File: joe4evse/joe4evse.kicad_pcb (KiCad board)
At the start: 2 copper layers, 100 x 100 mm, 74 parts, among them J1 USB_B_Micro, J10 Conn_01x02, J11 Conn_01x02, J2 Conn_01x03, J3 Conn_01x03, J4 Conn_01x02, J5 Conn_01x02, J6 CONNFLY_Elec_DS1129-04-S8B0P-X, J7 8P8C_LED_Shielded, J8 Conn_01x02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

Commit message: joe/pcb: Routing done
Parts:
- added REF**: Symbol_Highvoltage_Type1_CopperTop_Small, Symbol:Symbol_Highvoltage_Type1_CopperTop_Small, F.Cu at (182.4, 54.0)
- J5: value Conn_01x02 -> Conn_01x03; footprint Connector_JST:JST_NV_B02P-NV_1x02_P5.00mm_Vertical -> Connector_JST:JST_NV_B03P-NV_1x03_P5.00mm_Vertical
- moved J8 53.5 mm to (147.5, 77.9)
- moved D7 14.0 mm to (192.0, 114.0)
- moved D8 14.0 mm to (192.0, 106.0)
- moved D9 14.0 mm to (192.0, 98.0)
- moved J10 14.0 mm to (197.0, 106.0)
- moved J11 14.0 mm to (197.0, 98.0)
- moved J9 14.0 mm to (197.0, 114.0)
- moved Q1 14.0 mm to (189.0, 116.0)
- moved Q2 14.0 mm to (189.0, 108.0)
- moved Q3 14.0 mm to (189.0, 100.0)
- moved R7 14.0 mm to (189.0, 97.0)
- moved R8 14.0 mm to (189.0, 113.0)
- moved R9 14.0 mm to (189.0, 105.0)
- moved D11 10.0 mm to (176.0, 77.0)
- moved J5 10.0 mm to (194.0, 77.0)
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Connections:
- J5 pad 2: /evse/AC_TEST_IN1 -> /evse/AC_TEST_N
- U7 pad 2: GND -> /evse/AC_TEST_N
- U7 pad 3: GND -> /evse/AC_TEST_N
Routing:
- net +3V3: track 0.00 -> 292.6 mm, vias 0 -> 12
- net +12V: track 0.00 -> 179.3 mm, vias 0 -> 3
- net +5V: track 0.00 -> 167.6 mm, vias 0 -> 3
- net /RELAY_RCMB: track 0.00 -> 80.9 mm, vias 0 -> 2
- net /MOD_EN: track 0.00 -> 80.6 mm
- net /RELAY_JACK: track 0.00 -> 75.0 mm, vias 0 -> 4
- net /RELAY_AC: track 0.00 -> 74.1 mm, vias 0 -> 2
- net /evse/AC_TEST1: track 0.00 -> 73.9 mm
- net /NFC_~RST: track 0.00 -> 72.2 mm, vias 0 -> 2
- net /evse/AC_TEST0: track 0.00 -> 69.9 mm
- net /LED_~CS: track 0.00 -> 68.2 mm, vias 0 -> 2
- net /SCLK: track 0.00 -> 67.4 mm
- net /fipy/RCMB_AC_30mA: track 0.00 -> 66.6 mm
- net /NFC_IRQ: track 0.00 -> 66.2 mm, vias 0 -> 1
- net /NFC_~CS: track 0.00 -> 65.8 mm, vias 0 -> 2
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- added copper zone on B.Cu, net GND
- added copper zone on F.Cu, net GND
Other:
- outline, holes or cut-outs redrawn
- board text added: "A <-> B"
- board text added: "Dalton EVSE "Joe" Board rev. 1.0 (c) Tuetuopay 2019"
- board text added: "High voltage"
- board text added: "PP | Pilot"
- board text added: "RCMB relay AC cutoff relay EV Jack relay"
- board text added: "To Averell"
- board text added: "To William"

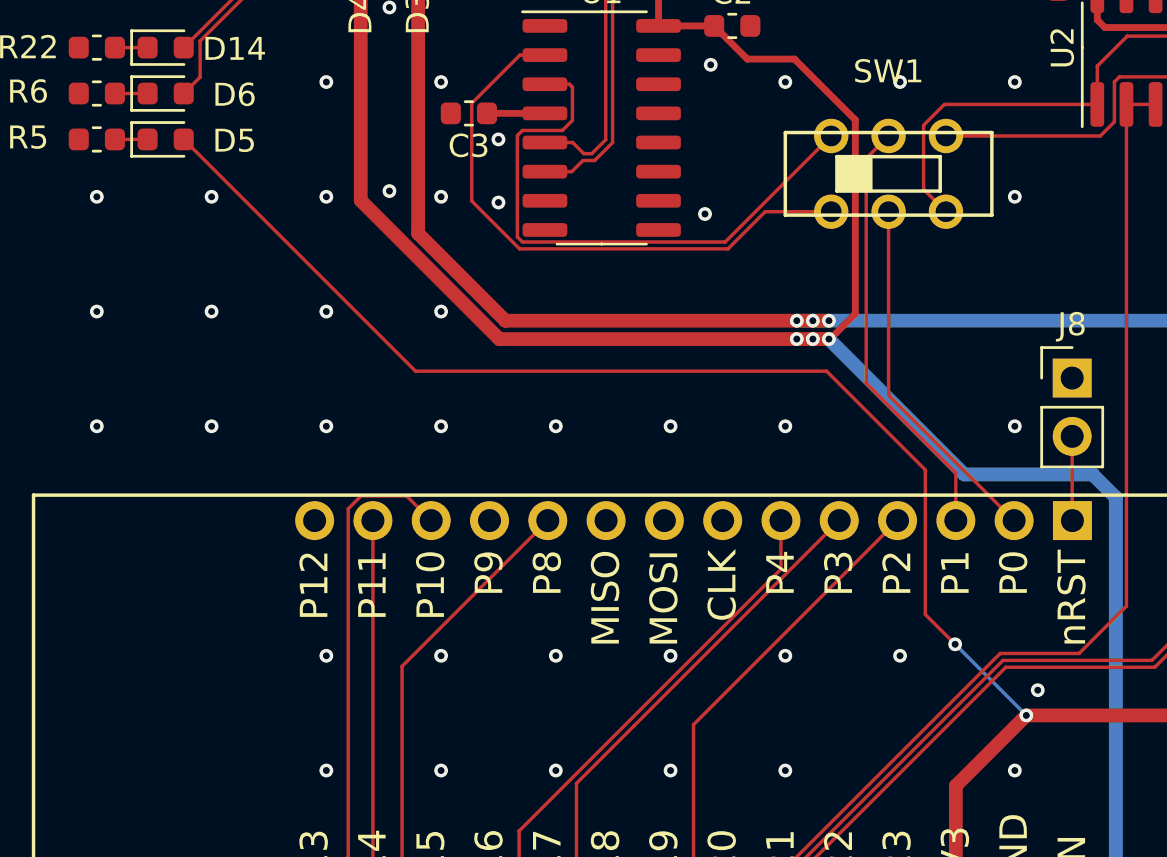
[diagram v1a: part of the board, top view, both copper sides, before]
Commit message: joe/{sch, pcb}: Add missing temp sensor
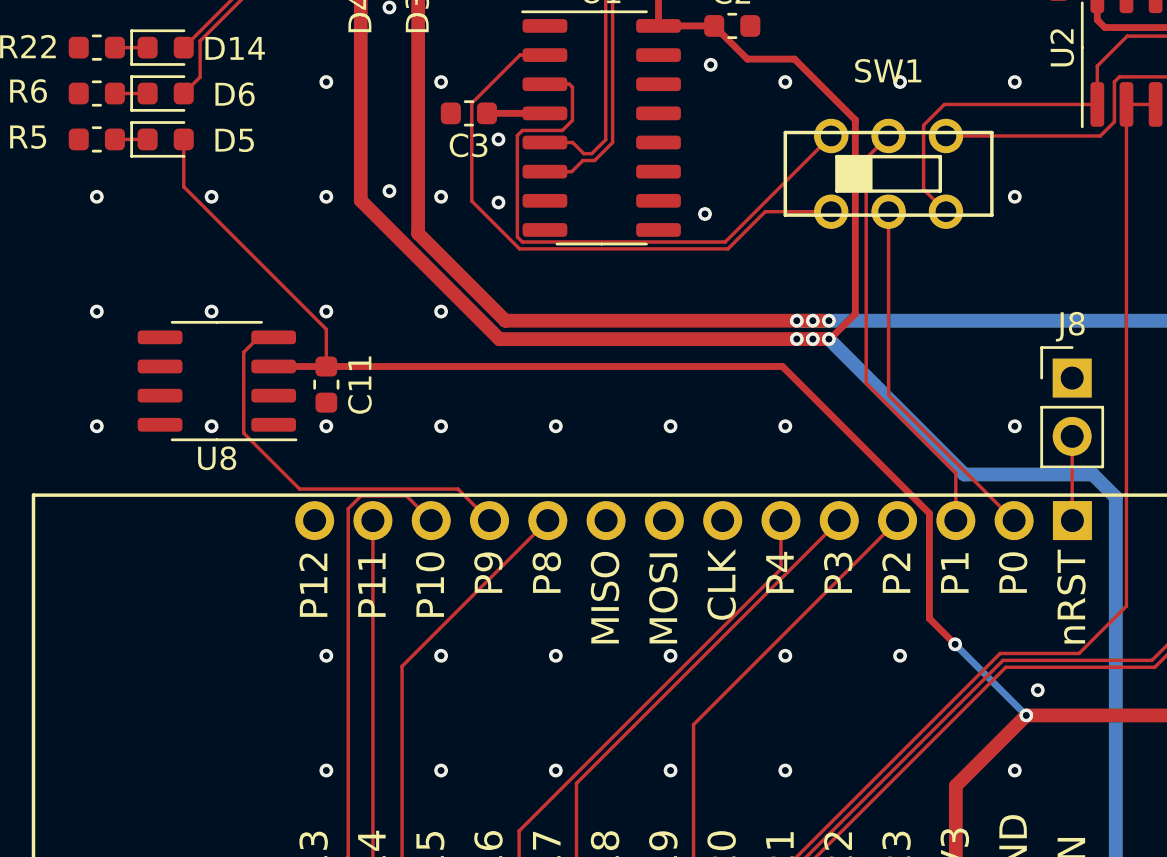
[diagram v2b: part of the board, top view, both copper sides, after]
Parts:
- added C11: 100n, Capacitor_SMD:C_0603_1608Metric, F.Cu at (115.0, 78.2)
- added U8: DS18B20Z, Package_SO:SOIC-8_3.9x4.9mm_P1.27mm, F.Cu at (110.2, 78.0)
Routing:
- net /fipy/TEMP: track 0.00 -> 17.4 mm
- net +3V3: track 292.6 -> 296.0 mm
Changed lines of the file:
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@@
     (thickness 1.6)
     (drawings 51)
-    (tracks 729)
+    (tracks 738)
     (zones 0)
-    (modules 76)
-    (nets 106)
+    (modules 78)
+    (nets 111)
   )
   (page A4)
@@
   (net 104 "Net-(D15-Pad2)")
   (net 105 /evse/AC_TEST_N)
+  (net 106 "Net-(U8-Pad8)")
+  (net 107 "Net-(U8-Pad7)")
+  (net 108 "Net-(U8-Pad6)")
+  (net 109 "Net-(U8-Pad2)")
+  (net 110 "Net-(U8-Pad1)")
   (net_class Default "This is the default net class."
     (clearance 0.15)
@@
     (add_net "Net-(U6-Pad5)")
     (add_net "Net-(U6-Pad8)")
+    (add_net "Net-(U8-Pad1)")
+    (add_net "Net-(U8-Pad2)")
+    (add_net "Net-(U8-Pad6)")
+    (add_net "Net-(U8-Pad7)")
+    (add_net "Net-(U8-Pad8)")
   )
   (net_class Power ""
@@
     (add_net -12V)
   )
+  (module Package_SO:SOIC-8_3.9x4.9mm_P1.27mm (layer F.Cu)
+    (at 110.23 78.03 180)
+    (descr "SOIC, 8 Pin (JEDEC MS-012AA, https://www.analog.com/media/en/package-pcb-resources/package/pkg_pdf/soic_narrow-r/r_8.pdf), generated with kicad-footprint-generator ipc_gullwing_generator.py")
+    (tags "SOIC SO")
+    (attr smd)
+    (fp_text reference U8 (at 0 -3.4) (layer F.SilkS)
+      (effects (font (size 1 1) (thickness 0.15)))
+    )
+    (fp_text value DS18B20Z (at 0 3.4) (layer F.Fab)
+      (effects (font (size 1 1) (thickness 0.15)))
+    )
+    (fp_text user %R (at 0 0) (layer F.Fab)
+      (effects (font (size 0.98 0.98) (thickness 0.15)))
+    )
+    (fp_line (start 3.7 -2.7) (end -3.7 -2.7) (layer F.CrtYd) (width 0.05))
+    (fp_line (start 3.7 2.7) (end 3.7 -2.7) (layer F.CrtYd) (width 0.05))
+    (fp_line (start -3.7 2.7) (end 3.7 2.7) (layer F.CrtYd) (width 0.05))
+    (fp_line (start -3.7 -2.7) (end -3.7 2.7) (layer F.CrtYd) (width 0.05))
+    (fp_line (start -1.95 -1.475) (end -0.975 -2.45) (layer F.Fab) (width 0.1))
+    (fp_line (start -1.95 2.45) (end -1.95 -1.475) (layer F.Fab) (width 0.1))
+    (fp_line (start 1.95 2.45) (end -1.95 2.45) (layer F.Fab) (width 0.1))
+    (fp_line (start 1.95 -2.45) (end 1.95 2.45) (layer F.Fab) (width 0.1))
+    (fp_line (start -0.975 -2.45) (end 1.95 -2.45) (layer F.Fab) (width 0.1))
+    (fp_line (start 0 -2.56) (end -3.45 -2.56) (layer F.SilkS) (width 0.12))
+    (fp_line (start 0 -2.56) (end 1.95 -2.56) (layer F.SilkS) (width 0.12))
+    (fp_line (start 0 2.56) (end -1.95 2.56) (layer F.SilkS) (width 0.12))
+    (fp_line (start 0 2.56) (end 1.95 2.56) (layer F.SilkS) (width 0.12))
+    (pad 8 smd roundrect (at 2.475 -1.905 180) (size 1.95 0.6) (layers F.Cu F.Paste F.Mask) (roundrect_rratio 0.25)
+      (net 106 "Net-(U8-Pad8)"))
+    (pad 7 smd roundrect (at 2.475 -0.635 180) (size 1.95 0.6) (layers F.Cu F.Paste F.Mask) (roundrect_rratio 0.25)
+      (net 107 "Net-(U8-Pad7)"))
+    (pad 6 smd roundrect (at 2.475 0.635 180) (size 1.95 0.6) (layers F.Cu F.Paste F.Mask) (roundrect_rratio 0.25)
+      (net 108 "Net-(U8-Pad6)"))
+    (pad 5 smd roundrect (at 2.475 1.905 180) (size 1.95 0.6) (layers F.Cu F.Paste F.Mask) (roundrect_rratio 0.25)
+      (net 2 GND))
+    (pad 4 smd roundrect (at -2.475 1.905 180) (size 1.95 0.6) (layers F.Cu F.Paste F.Mask) (roundrect_rratio 0.25)
+      (net 88 /fipy/TEMP))
+    (pad 3 smd roundrect (at -2.475 0.635 180) (size 1.95 0.6) (layers F.Cu F.Paste F.Mask) (roundrect_rratio 0.25)
+      (net 1 +3V3))
+    (pad 2 smd roundrect (at -2.475 -0.635 180) (size 1.95 0.6) (layers F.Cu F.Paste F.Mask) (roundrect_rratio 0.25)
+      (net 109 "Net-(U8-Pad2)"))
+    (pad 1 smd roundrect (at -2.475 -1.905 180) (size 1.95 0.6) (layers F.Cu F.Paste F.Mask) (roundrect_rratio 0.25)
+      (net 110 "Net-(U8-Pad1)"))
+    (model ${KISYS3DMOD}/Package_SO.3dshapes/SOIC-8_3.9x4.9mm_P1.27mm.wrl
+      (at (xyz 0 0 0))
+      (scale (xyz 1 1 1))
+      (rotate (xyz 0 0 0))
+    )
+  )
+  (module Capacitor_SMD:C_0603_1608Metric (layer F.Cu)
+    (at 115 78.1825 90)
+    (descr "Capacitor SMD 0603 (1608 Metric), square (rectangular) end terminal, IPC_7351 nominal, (Body size source: http://www.tortai-tech.com/upload/download/2011102023233369053.pdf), generated with kicad-footprint-generator")
+    (tags capacitor)
+    (attr smd)
+    (fp_text reference C11 (at 0 1.5 90) (layer F.SilkS)
+      (effects (font (size 1 1) (thickness 0.15)))
+    )
+    (fp_text value 100n (at 0 1.43 90) (layer F.Fab)
+      (effects (font (size 1 1) (thickness 0.15)))
+    )
+    (fp_text user %R (at 0 0 90) (layer F.Fab)
+      (effects (font (size 0.4 0.4) (thickness 0.06)))
+    )
+    (fp_line (start 1.48 0.73) (end -1.48 0.73) (layer F.CrtYd) (width 0.05))
+    (fp_line (start 1.48 -0.73) (end 1.48 0.73) (layer F.CrtYd) (width 0.05))
+    (fp_line (start -1.48 -0.73) (end 1.48 -0.73) (layer F.CrtYd) (width 0.05))
+    (fp_line (start -1.48 0.73) (end -1.48 -0.73) (layer F.CrtYd) (width 0.05))
+    (fp_line (start -0.162779 0.51) (end 0.162779 0.51) (layer F.SilkS) (width 0.12))
+    (fp_line (start -0.162779 -0.51) (end 0.162779 -0.51) (layer F.SilkS) (width 0.12))
+    (fp_line (start 0.8 0.4) (end -0.8 0.4) (layer F.Fab) (width 0.1))
+    (fp_line (start 0.8 -0.4) (end 0.8 0.4) (layer F.Fab) (width 0.1))
+    (fp_line (start -0.8 -0.4) (end 0.8 -0.4) (layer F.Fab) (width 0.1))
+    (fp_line (start -0.8 0.4) (end -0.8 -0.4) (layer F.Fab) (width 0.1))
+    (pad 2 smd roundrect (at 0.7875 0 90) (size 0.875 0.95) (layers F.Cu F.Paste F.Mask) (roundrect_rratio 0.25)
+      (net 1 +3V3))
+    (pad 1 smd roundrect (at -0.7875 0 90) (size 0.875 0.95) (layers F.Cu F.Paste F.Mask) (roundrect_rratio 0.25)
+      (net 2 GND))
+    (model ${KISYS3DMOD}/Capacitor_SMD.3dshapes/C_0603_1608Metric.wrl
+      (at (xyz 0 0 0))
+      (scale (xyz 1 1 1))
+      (rotate (xyz 0 0 0))
+    )
+  )
   (module Symbol:Symbol_Highvoltage_Type1_CopperTop_Small locked (layer F.Cu)
     (at 182.4 54)
@@
   (via (at 145.5 92.6) (size 0.6) (drill 0.3) (layers F.Cu B.Cu) (net 1))
   (via (at 142.4 89.5) (size 0.6) (drill 0.3) (layers F.Cu B.Cu) (net 1))
-  (segment (start 145.5 92.6) (end 142.4 89.5) (width 0.15) (layer B.Cu) (net 1))
-  (segment (start 142.4 89.5) (end 141.1 88.2) (width 0.15) (layer F.Cu) (net 1))
-  (segment (start 141.1 88.2) (end 141.1 81.9) (width 0.15) (layer F.Cu) (net 1))
-  (segment (start 141.1 81.9) (end 136.8 77.6) (width 0.15) (layer F.Cu) (net 1))
-  (segment (start 118.8875 77.6) (end 108.7875 67.5) (width 0.15) (layer F.Cu) (net 1))
-  (segment (start 136.8 77.6) (end 118.8875 77.6) (width 0.15) (layer F.Cu) (net 1))
   (segment (start 189.7875 97) (end 184.1875 91.4) (width 0.3) (layer F.Cu) (net 1))
   (segment (start 169.7 91.4) (end 161.9 83.6) (width 0.3) (layer F.Cu) (net 1))
   (segment (start 184.1875 91.4) (end 169.7 91.4) (width 0.3) (layer F.Cu) (net 1))
   (segment (start 132.385 141.055) (end 133.405 142.835) (width 0.6) (layer B.Cu) (net 1))
+  (segment (start 112.705 77.395) (end 115 77.395) (width 0.3) (layer F.Cu) (net 1))
+  (segment (start 141.279999 88.379999) (end 142.4 89.5) (width 0.3) (layer F.Cu) (net 1))
+  (segment (start 141.279999 83.797997) (end 141.279999 88.379999) (width 0.3) (layer F.Cu) (net 1))
+  (segment (start 134.877002 77.395) (end 141.279999 83.797997) (width 0.3) (layer F.Cu) (net 1))
+  (segment (start 115 77.395) (end 134.877002 77.395) (width 0.3) (layer F.Cu) (net 1))
+  (segment (start 142.4 89.5) (end 145.5 92.6) (width 0.3) (layer B.Cu) (net 1))
+  (segment (start 115 75.777002) (end 115 77.395) (width 0.15) (layer F.Cu) (net 1))
+  (segment (start 108.7875 69.564502) (end 115 75.777002) (width 0.15) (layer F.Cu) (net 1))
+  (segment (start 108.7875 67.5) (end 108.7875 69.564502) (width 0.15) (layer F.Cu) (net 1))
   (via (at 105 60) (size 0.6) (drill 0.3) (layers F.Cu B.Cu) (net 2))
   (via (at 110 60) (size 0.6) (drill 0.3) (layers F.Cu B.Cu) (net 2))
@@
   (segment (start 120.39999 103.60001) (end 122.11 101.89) (width 0.15) (layer F.Cu) (net 85))
   (segment (start 116.168546 103.60001) (end 120.39999 103.60001) (width 0.15) (layer F.Cu) (net 85))
+  (segment (start 120.734989 82.734989) (end 122.11 84.11) (width 0.15) (layer F.Cu) (net 88))
+  (segment (start 112.05 76.125) (end 111.4 76.775) (width 0.15) (layer F.Cu) (net 88))
+  (segment (start 111.4 80.3) (end 113.834989 82.734989) (width 0.15) (layer F.Cu) (net 88))
+  (segment (start 112.705 76.125) (end 112.05 76.125) (width 0.15) (layer F.Cu) (net 88))
+  (segment (start 113.834989 82.734989) (end 120.734989 82.734989) (width 0.15) (layer F.Cu) (net 88))
+  (segment (start 111.4 76.775) (end 111.4 80.3) (width 0.15) (layer F.Cu) (net 88))
   (segment (start 118.3 102.405501) (end 118.3 90.46) (width 0.15) (layer F.Cu) (net 89))
   (segment (start 117.405501 103.3) (end 118.3 102.405501) (width 0.15) (layer F.Cu) (net 89))

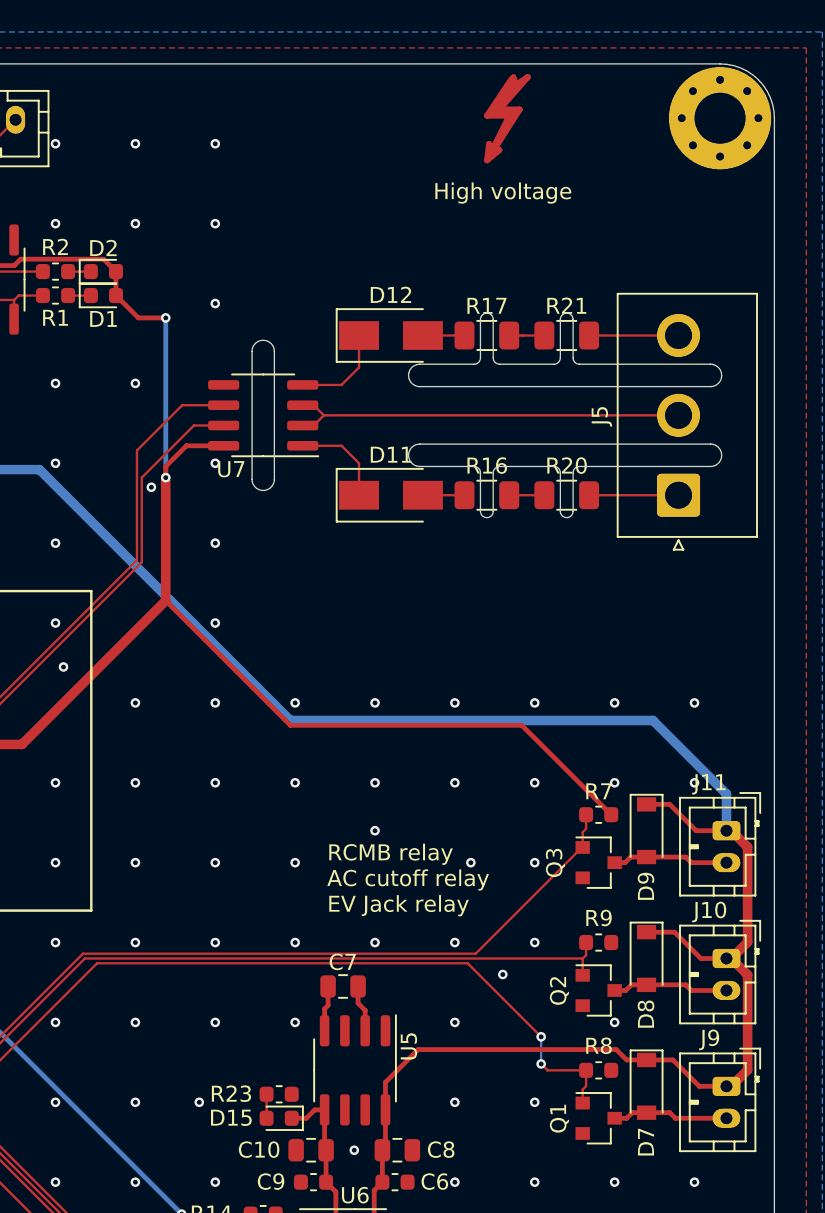
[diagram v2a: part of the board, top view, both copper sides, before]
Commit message: joe: Add temperature sensor
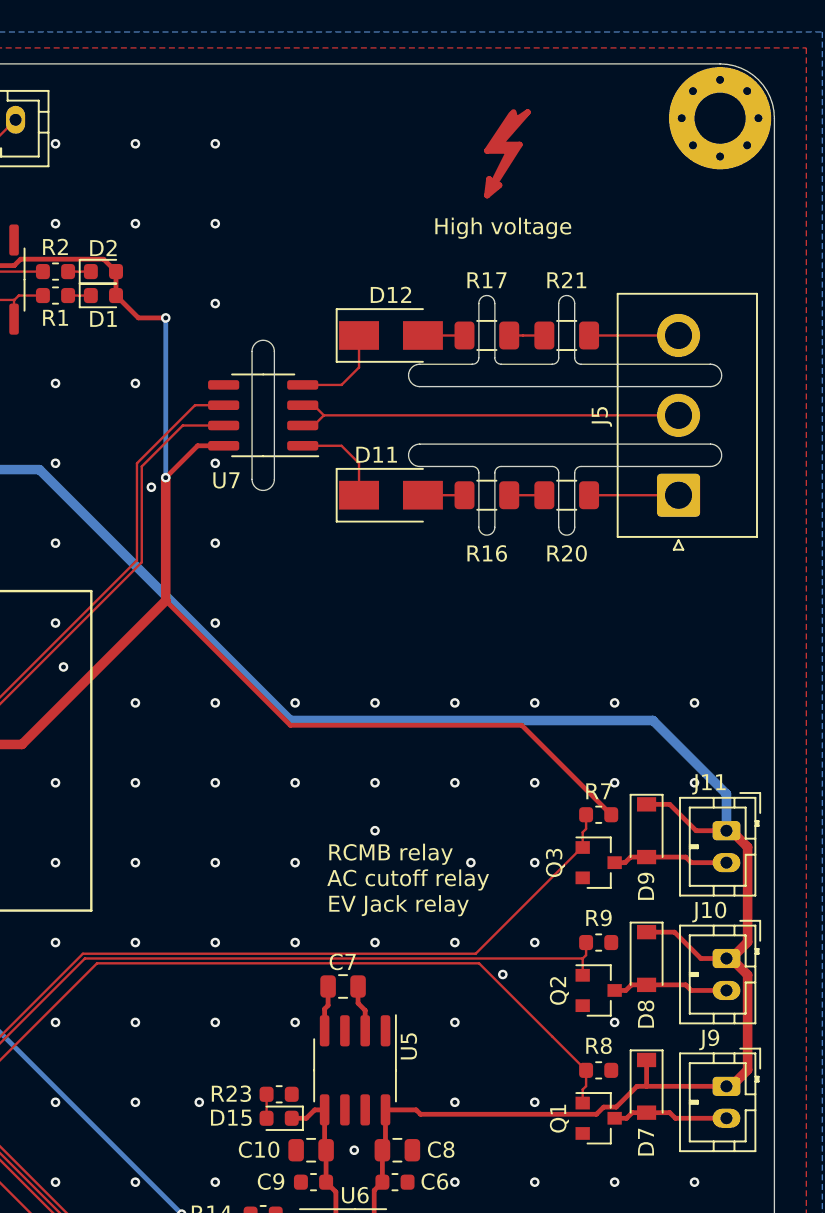
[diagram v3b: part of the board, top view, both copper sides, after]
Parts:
- moved REF** 2.20 mm to (182.4, 56.2)
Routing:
- net +12V: track 179.3 -> 178.3 mm
- net /RELAY_JACK: track 75.0 -> 74.0 mm, vias 4 -> 2
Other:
- outline, holes or cut-outs redrawn
